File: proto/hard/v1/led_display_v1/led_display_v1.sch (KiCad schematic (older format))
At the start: 97 parts, among them U1 LCD_2.8_SPI, U2 74HCT595, U3 74HCT595, U4 74HCT595

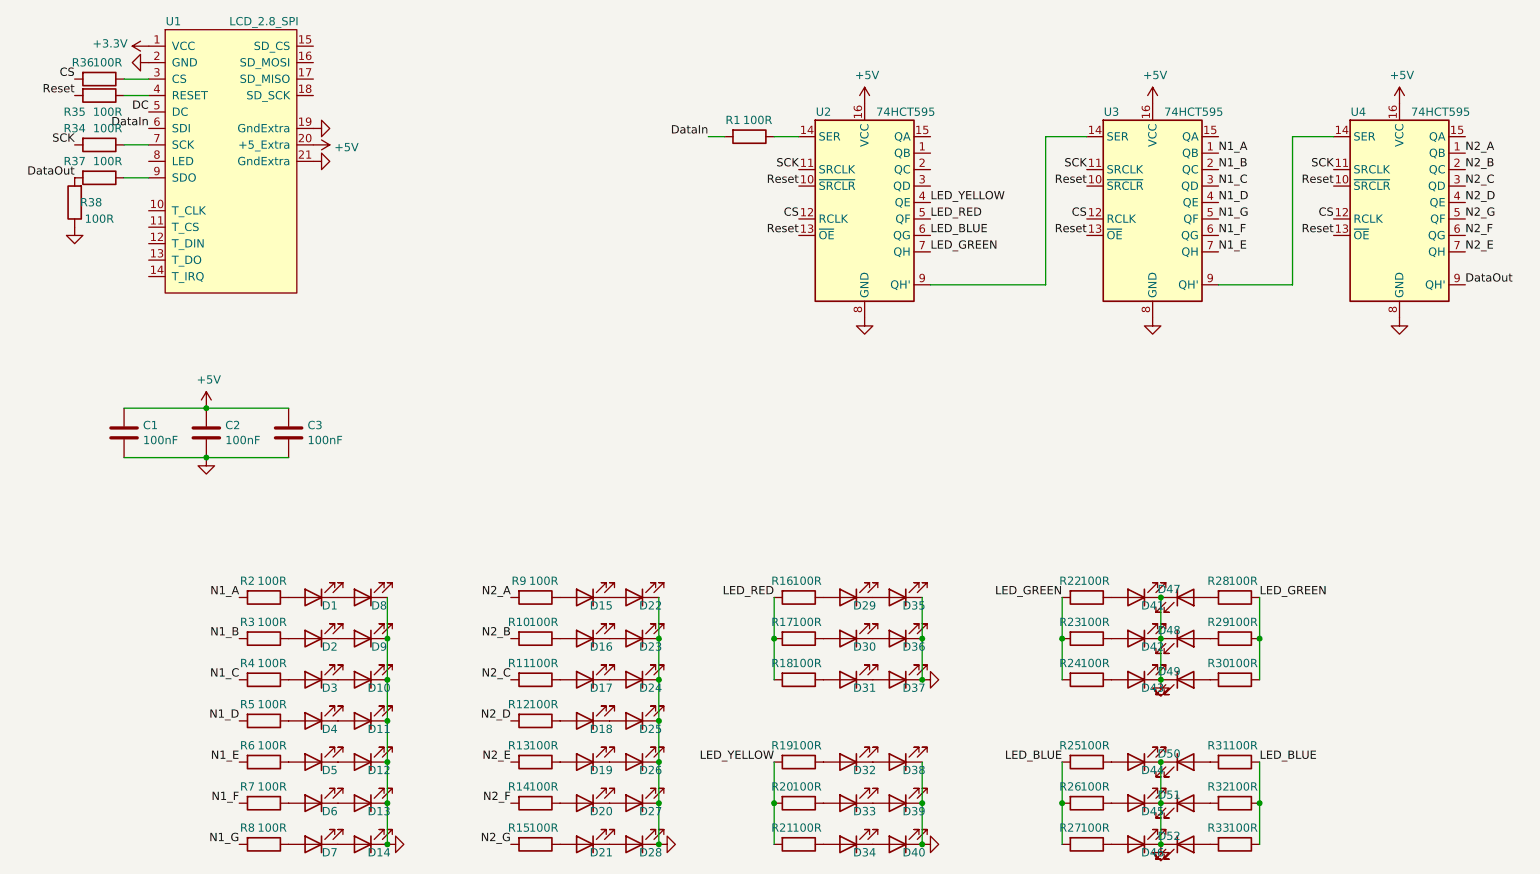
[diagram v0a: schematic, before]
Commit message: Started implementation of LED display ctrl. Fixed wrong segments naming on led_display board.
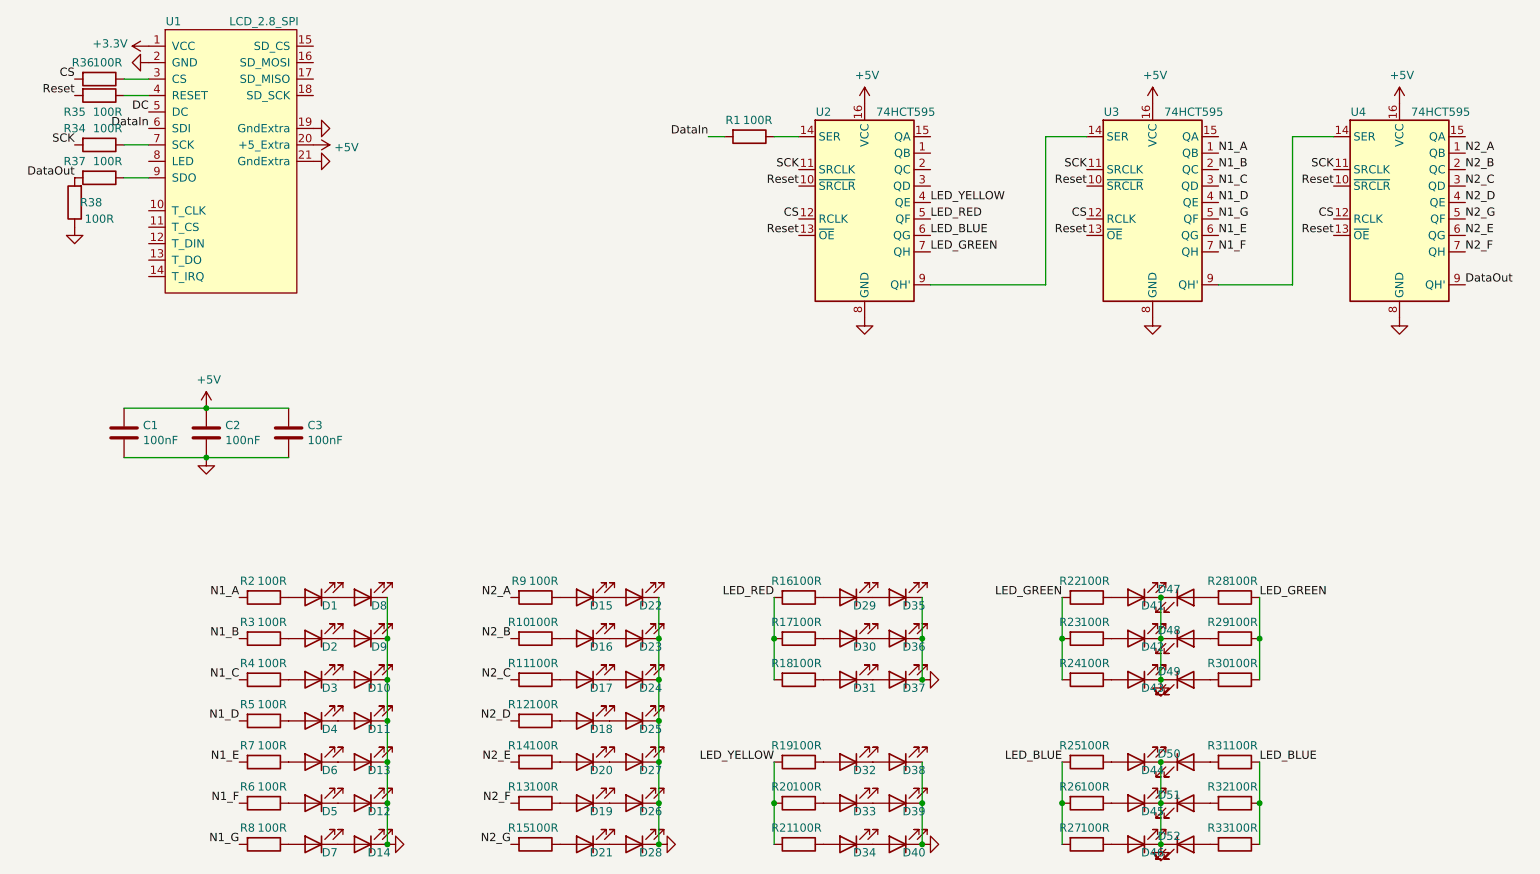
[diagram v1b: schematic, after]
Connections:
- net N1_E: now also R7.2, U3.6 (QG); no longer R6.2, U3.7 (QH)
- net N1_F: now also R6.2, U3.7 (QH); no longer R7.2, U3.6 (QG)
- net N2_E: now also R14.2, U4.6 (QG); no longer R13.2, U4.7 (QH)
- net N2_F: now also R13.2, U4.7 (QH); no longer R14.2, U4.6 (QG)
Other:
- moved on the sheet: D12, D13, D19, D20, D26, D27, D5, D6, R13, R14, R6, R7
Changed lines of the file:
@@
 L Device:LED D12
 U 1 1 5EBD78D7
+P 2700 5700
+F 0 "D12" H 2600 5750 50  0000 C CNN
+F 1 "LED" H 2693 5825 50  0001 C CNN
+F 2 "LED_SMD:LED_0805_2012Metric" H 2700 5700 50  0001 C CNN
+F 3 "~" H 2700 5700 50  0001 C CNN
+	1    2700 5700
+	-1   0    0    1
+$EndComp
+$Comp
+L Device:LED D5
+U 1 1 5EBD78DD
+P 2400 5700
+F 0 "D5" H 2300 5750 50  0000 C CNN
+F 1 "LED" H 2393 5825 50  0001 C CNN
+F 2 "LED_SMD:LED_0805_2012Metric" H 2400 5700 50  0001 C CNN
+F 3 "~" H 2400 5700 50  0001 C CNN
+	1    2400 5700
+	-1   0    0    1
+$EndComp
+$Comp
+L Device:LED D13
+U 1 1 5EBD78E3
 P 2700 5450
-F 0 "D12" H 2600 5500 50  0000 C CNN
+F 0 "D13" H 2600 5500 50  0000 C CNN
 F 1 "LED" H 2693 5575 50  0001 C CNN
 F 2 "LED_SMD:LED_0805_2012Metric" H 2700 5450 50  0001 C CNN
@@
 $EndComp
 $Comp
-L Device:LED D5
-U 1 1 5EBD78DD
+L Device:LED D6
+U 1 1 5EBD78E9
 P 2400 5450
-F 0 "D5" H 2300 5500 50  0000 C CNN
+F 0 "D6" H 2300 5500 50  0000 C CNN
 F 1 "LED" H 2393 5575 50  0001 C CNN
 F 2 "LED_SMD:LED_0805_2012Metric" H 2400 5450 50  0001 C CNN
 F 3 "~" H 2400 5450 50  0001 C CNN
 	1    2400 5450
-	-1   0    0    1
-$EndComp
-$Comp
-L Device:LED D13
-U 1 1 5EBD78E3
-P 2700 5700
-F 0 "D13" H 2600 5750 50  0000 C CNN
-F 1 "LED" H 2693 5825 50  0001 C CNN
-F 2 "LED_SMD:LED_0805_2012Metric" H 2700 5700 50  0001 C CNN
-F 3 "~" H 2700 5700 50  0001 C CNN
-	1    2700 5700
-	-1   0    0    1
-$EndComp
-$Comp
-L Device:LED D6
-U 1 1 5EBD78E9
-P 2400 5700
-F 0 "D6" H 2300 5750 50  0000 C CNN
-F 1 "LED" H 2393 5825 50  0001 C CNN
-F 2 "LED_SMD:LED_0805_2012Metric" H 2400 5700 50  0001 C CNN
-F 3 "~" H 2400 5700 50  0001 C CNN
-	1    2400 5700
 	-1   0    0    1
 $EndComp
@@
 L Device:R R6
 U 1 1 5EBE8731
+P 2100 5700
+F 0 "R6" V 2000 5600 50  0000 C CNN
+F 1 "100R" V 2000 5750 50  0000 C CNN
+F 2 "Resistor_SMD:R_0805_2012Metric" V 2030 5700 50  0001 C CNN
+F 3 "~" H 2100 5700 50  0001 C CNN
+	1    2100 5700
+	0    1    1    0
+$EndComp
+$Comp
+L Device:R R7
+U 1 1 5EBE8A0E
 P 2100 5450
-F 0 "R6" V 2000 5350 50  0000 C CNN
+F 0 "R7" V 2000 5350 50  0000 C CNN
 F 1 "100R" V 2000 5500 50  0000 C CNN
 F 2 "Resistor_SMD:R_0805_2012Metric" V 2030 5450 50  0001 C CNN
 F 3 "~" H 2100 5450 50  0001 C CNN
 	1    2100 5450
-	0    1    1    0
-$EndComp
-$Comp
-L Device:R R7
-U 1 1 5EBE8A0E
-P 2100 5700
-F 0 "R7" V 2000 5600 50  0000 C CNN
-F 1 "100R" V 2000 5750 50  0000 C CNN
-F 2 "Resistor_SMD:R_0805_2012Metric" V 2030 5700 50  0001 C CNN
-F 3 "~" H 2100 5700 50  0001 C CNN
-	1    2100 5700
 	0    1    1    0
 $EndComp
@@
 L Device:LED D26
 U 1 1 5EC38358
+P 4350 5700
+F 0 "D26" H 4250 5750 50  0000 C CNN
+F 1 "LED" H 4343 5825 50  0001 C CNN
+F 2 "LED_SMD:LED_0805_2012Metric" H 4350 5700 50  0001 C CNN
+F 3 "~" H 4350 5700 50  0001 C CNN
+	1    4350 5700
+	-1   0    0    1
+$EndComp
+$Comp
+L Device:LED D19
+U 1 1 5EC3835E
+P 4050 5700
+F 0 "D19" H 3950 5750 50  0000 C CNN
+F 1 "LED" H 4043 5825 50  0001 C CNN
+F 2 "LED_SMD:LED_0805_2012Metric" H 4050 5700 50  0001 C CNN
+F 3 "~" H 4050 5700 50  0001 C CNN
+	1    4050 5700
+	-1   0    0    1
+$EndComp
+$Comp
+L Device:LED D27
+U 1 1 5EC38364
 P 4350 5450
-F 0 "D26" H 4250 5500 50  0000 C CNN
+F 0 "D27" H 4250 5500 50  0000 C CNN
 F 1 "LED" H 4343 5575 50  0001 C CNN
 F 2 "LED_SMD:LED_0805_2012Metric" H 4350 5450 50  0001 C CNN
@@
 $EndComp
 $Comp
-L Device:LED D19
-U 1 1 5EC3835E
+L Device:LED D20
+U 1 1 5EC3836A
 P 4050 5450
-F 0 "D19" H 3950 5500 50  0000 C CNN
+F 0 "D20" H 3950 5500 50  0000 C CNN
 F 1 "LED" H 4043 5575 50  0001 C CNN
 F 2 "LED_SMD:LED_0805_2012Metric" H 4050 5450 50  0001 C CNN
 F 3 "~" H 4050 5450 50  0001 C CNN
 	1    4050 5450
-	-1   0    0    1
-$EndComp
-$Comp
-L Device:LED D27
-U 1 1 5EC38364
-P 4350 5700
-F 0 "D27" H 4250 5750 50  0000 C CNN
-F 1 "LED" H 4343 5825 50  0001 C CNN
-F 2 "LED_SMD:LED_0805_2012Metric" H 4350 5700 50  0001 C CNN
-F 3 "~" H 4350 5700 50  0001 C CNN
-	1    4350 5700
-	-1   0    0    1
-$EndComp
-$Comp
-L Device:LED D20
-U 1 1 5EC3836A
-P 4050 5700
-F 0 "D20" H 3950 5750 50  0000 C CNN
-F 1 "LED" H 4043 5825 50  0001 C CNN
-F 2 "LED_SMD:LED_0805_2012Metric" H 4050 5700 50  0001 C CNN
-F 3 "~" H 4050 5700 50  0001 C CNN
-	1    4050 5700
 	-1   0    0    1
 $EndComp
@@
 L Device:R R13
 U 1 1 5EC3839F
+P 3750 5700
+F 0 "R13" V 3650 5600 50  0000 C CNN
+F 1 "100R" V 3650 5750 50  0000 C CNN
+F 2 "Resistor_SMD:R_0805_2012Metric" V 3680 5700 50  0001 C CNN
+F 3 "~" H 3750 5700 50  0001 C CNN
+	1    3750 5700
+	0    1    1    0
+$EndComp
+$Comp
+L Device:R R14
+U 1 1 5EC383A5
 P 3750 5450
-F 0 "R13" V 3650 5350 50  0000 C CNN
+F 0 "R14" V 3650 5350 50  0000 C CNN
 F 1 "100R" V 3650 5500 50  0000 C CNN
 F 2 "Resistor_SMD:R_0805_2012Metric" V 3680 5450 50  0001 C CNN
 F 3 "~" H 3750 5450 50  0001 C CNN
 	1    3750 5450
-	0    1    1    0
-$EndComp
-$Comp
-L Device:R R14
-U 1 1 5EC383A5
-P 3750 5700
-F 0 "R14" V 3650 5600 50  0000 C CNN
-F 1 "100R" V 3650 5750 50  0000 C CNN
-F 2 "Resistor_SMD:R_0805_2012Metric" V 3680 5700 50  0001 C CNN
-F 3 "~" H 3750 5700 50  0001 C CNN
-	1    3750 5700
 	0    1    1    0
 $EndComp
@@
 	2850 4950 2850 5200
 Connection ~ 2850 5200
-Wire Wire Line
-	2850 5200 2850 5450
-Connection ~ 2850 5450
-Wire Wire Line
-	2850 5450 2850 5700
-Connection ~ 2850 5700
-Wire Wire Line
-	2850 5700 2850 5950
 $Comp
 L power:GND #PWR0112
@@
 	4500 4950 4500 5200
 Connection ~ 4500 5200
-Wire Wire Line
-	4500 5200 4500 5450
-Connection ~ 4500 5450
-Wire Wire Line
-	4500 5450 4500 5700
-Connection ~ 4500 5700
-Wire Wire Line
-	4500 5700 4500 5950
 $Comp
 L power:GND #PWR0113
@@
 Text Label 9400 2050 0    50   ~ 0
 N2_D
+Text Label 9400 2250 0    50   ~ 0
+N2_E
 Text Label 9400 2350 0    50   ~ 0
-N2_E
-Text Label 9400 2250 0    50   ~ 0
 N2_F
 Text Label 9400 2150 0    50   ~ 0
@@
 Text Label 7900 2050 0    50   ~ 0
 N1_D
+Text Label 7900 2250 0    50   ~ 0
+N1_E
 Text Label 7900 2350 0    50   ~ 0
-N1_E
-Text Label 7900 2250 0    50   ~ 0
 N1_F
 Text Label 7900 2150 0    50   ~ 0
@@
 	1    0    0    -1
 $EndComp
+Connection ~ 2850 5700
+Wire Wire Line
+	2850 5700 2850 5950
+Wire Wire Line
+	2850 5200 2850 5450
+Connection ~ 2850 5450
+Wire Wire Line
+	2850 5450 2850 5700
+Connection ~ 4500 5700
+Wire Wire Line
+	4500 5700 4500 5950
+Wire Wire Line
+	4500 5200 4500 5450
+Connection ~ 4500 5450
+Wire Wire Line
+	4500 5450 4500 5700
 $EndSCHEMATC

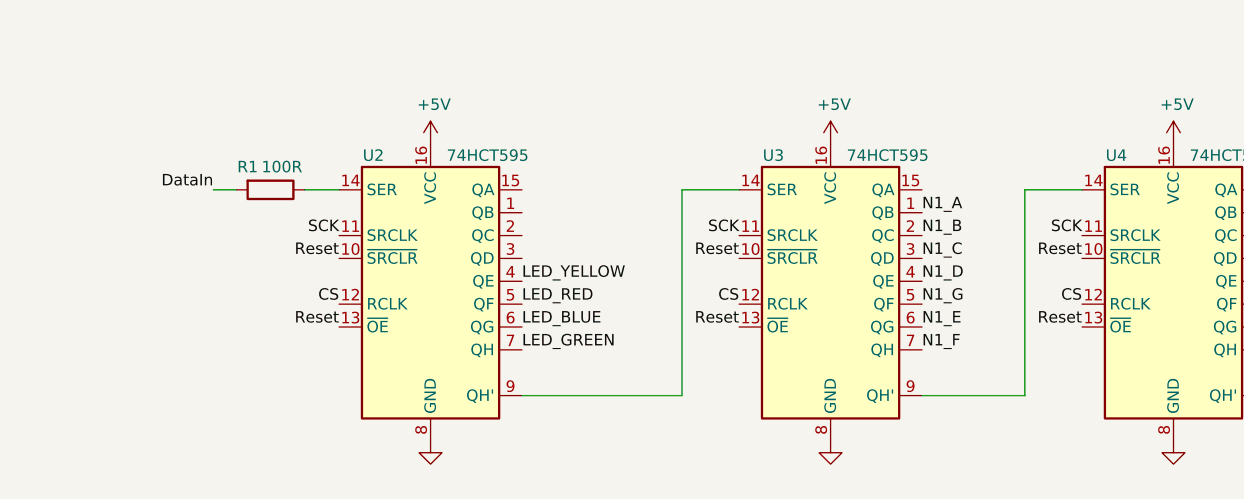
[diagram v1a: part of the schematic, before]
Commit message: Change SRCLR pin connection to external resistor pulled to +5. Board version increment to 0.2.
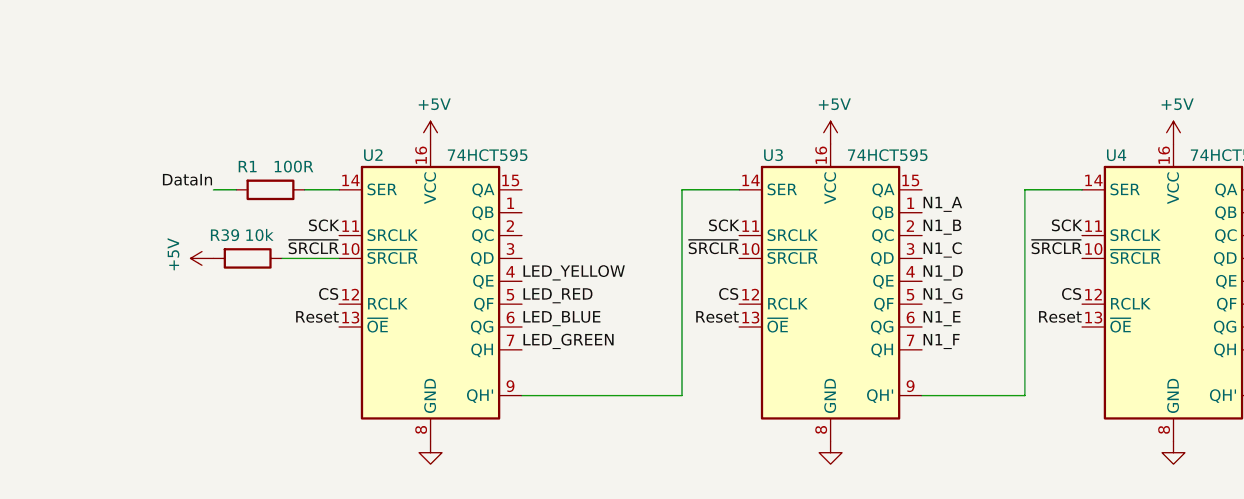
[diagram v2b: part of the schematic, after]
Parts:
- added R39: 10k, Resistor_SMD:R_0805_2012Metric, symbol Device:R
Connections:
- net +5V: now also R39.2
- net Reset: no longer U2.10 (~SRCLR), U3.10 (~SRCLR), U4.10 (~SRCLR)
- new net ~SRCLR: R39.1, U2.10 (~SRCLR), U3.10 (~SRCLR), U4.10 (~SRCLR)
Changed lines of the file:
@@
 P 5050 1650
 F 0 "R1" V 4950 1550 50  0000 C CNN
-F 1 "100R" V 4950 1700 50  0000 C CNN
+F 1 "100R" V 4950 1750 50  0000 C CNN
 F 2 "Resistor_SMD:R_0805_2012Metric" V 4980 1650 50  0001 C CNN
 F 3 "~" H 5050 1650 50  0001 C CNN
@@
 Wire Wire Line
 	4900 1650 4800 1650
-Text Label 5350 1950 2    50   ~ 0
-Reset
-Text Label 7100 1950 2    50   ~ 0
-Reset
-Text Label 8600 1950 2    50   ~ 0
-Reset
 $Comp
 L Device:LED D8
@@
 Wire Wire Line
 	4500 5450 4500 5700
+Text Label 5350 1950 2    50   ~ 0
+~SRCLR
+Text Label 7100 1950 2    50   ~ 0
+~SRCLR
+Text Label 8600 1950 2    50   ~ 0
+~SRCLR
+$Comp
+L Device:R R39
+U 1 1 6061CF47
+P 4950 1950
+F 0 "R39" V 4850 1850 50  0000 C CNN
+F 1 "10k" V 4850 2000 50  0000 C CNN
+F 2 "Resistor_SMD:R_0805_2012Metric" V 4880 1950 50  0001 C CNN
+F 3 "~" H 4950 1950 50  0001 C CNN
+	1    4950 1950
+	0    1    1    0
+$EndComp
+Wire Wire Line
+	5100 1950 5350 1950
+$Comp
+L power:+5V #PWR0121
+U 1 1 6061EB13
+P 4800 1950
+F 0 "#PWR0121" H 4800 1800 50  0001 C CNN
+F 1 "+5V" H 4815 2123 50  0000 C CNN
+F 2 "" H 4800 1950 50  0001 C CNN
+F 3 "" H 4800 1950 50  0001 C CNN
+	1    4800 1950
+	0    -1   -1   0
+$EndComp
 $EndSCHEMATC
